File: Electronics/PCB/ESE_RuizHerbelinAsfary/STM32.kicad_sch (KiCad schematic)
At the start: 0 parts

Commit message: STM32 Symbol finished
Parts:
- added U?: STM32G070RBTx, symbol STM32G070RBTx:STM32G070RBTx
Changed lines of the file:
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@@
 (kicad_sch (version 20211123) (generator eeschema)
   (paper "A4")
+  (symbol (lib_id "STM32G070RBTx:STM32G070RBTx") (at 96.52 52.07 0) (unit 1)
+    (in_bom yes) (on_board yes)
+    (property "Reference" "U?" (id 0) (at 49.53 29.21 0))
+    (property "Value" "STM32G070RBTx" (id 1) (at 55.88 77.47 0))
+    (property "Footprint" "" (id 2) (at 96.52 52.07 0)
+      (effects (font (size 1.27 1.27)) hide)
+    )
+    (property "Datasheet" "" (id 3) (at 96.52 52.07 0)
+      (effects (font (size 1.27 1.27)) hide)
+    )
+    (pin "1")
+    (pin "10")
+    (pin "11")
+    (pin "12")
+    (pin "13")
+    (pin "14")
+    (pin "15")
+    (pin "16")
+    (pin "17")
+    (pin "18")
+    (pin "19")
+    (pin "2")
+    (pin "20")
+    (pin "21")
+    (pin "22")
+    (pin "23")
+    (pin "24")
+    (pin "25")
+    (pin "26")
+    (pin "27")
+    (pin "28")
+    (pin "29")
+    (pin "3")
+    (pin "30")
+    (pin "31")
+    (pin "32")
+    (pin "33")
+    (pin "34")
+    (pin "35")
+    (pin "36")
+    (pin "37")
+    (pin "38")
+    (pin "39")
+    (pin "4")
+    (pin "40")
+    (pin "41")
+    (pin "42")
+    (pin "43")
+    (pin "44")
+    (pin "45")
+    (pin "46")
+    (pin "47")
+    (pin "48")
+    (pin "49")
+    (pin "5")
+    (pin "50")
+    (pin "51")
+    (pin "52")
+    (pin "53")
+    (pin "54")
+    (pin "55")
+    (pin "56")
+    (pin "57")
+    (pin "58")
+    (pin "59")
+    (pin "6")
+    (pin "60")
+    (pin "61")
+    (pin "62")
+    (pin "63")
+    (pin "64")
+    (pin "7")
+    (pin "8")
+    (pin "9")
+  )
 )

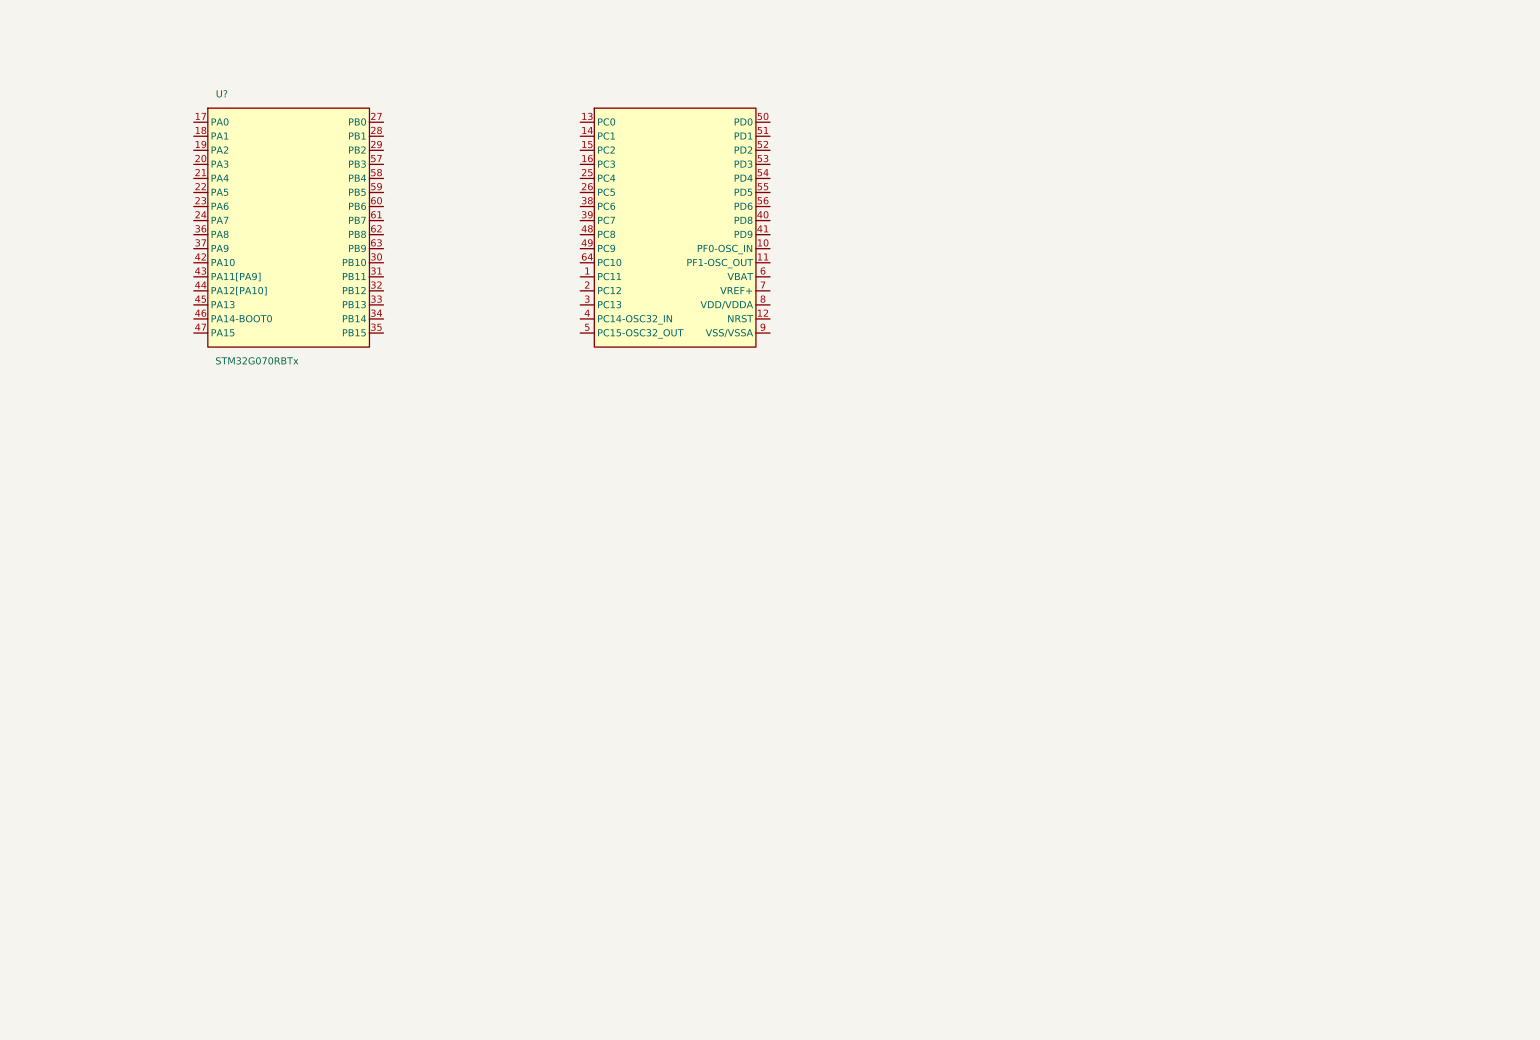
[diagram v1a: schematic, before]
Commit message: SWD connection finished
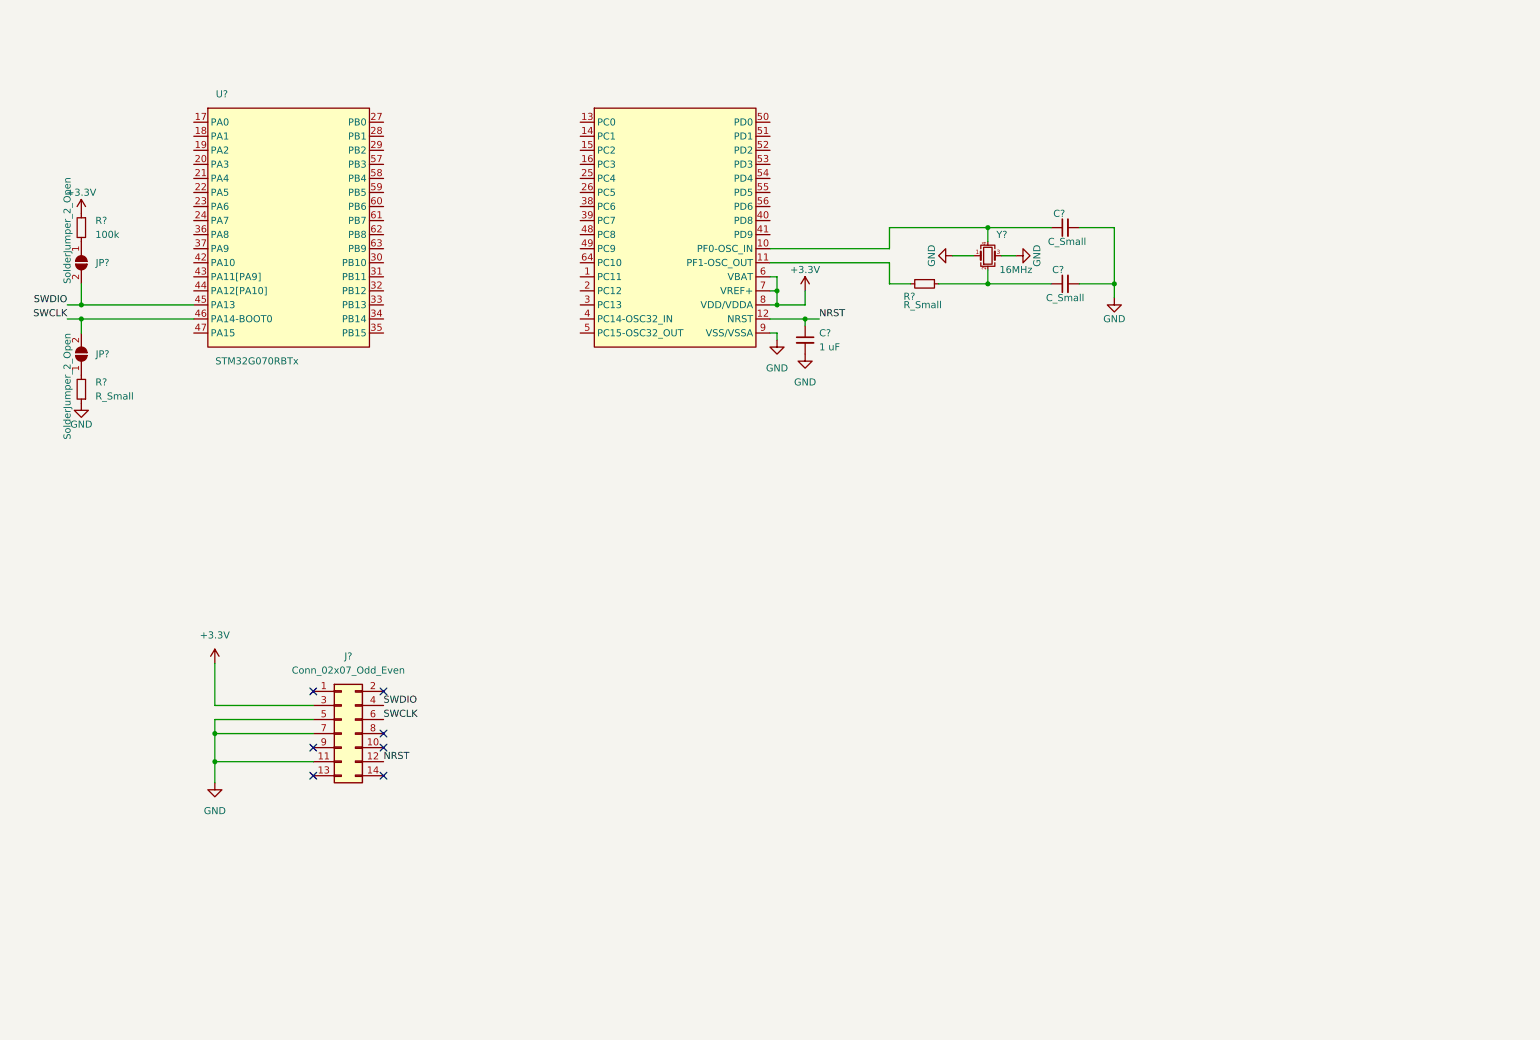
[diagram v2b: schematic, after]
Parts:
- added C? (x2): C_Small, Capacitor_SMD:C_0603_1608Metric_Pad1.08x0.95mm_HandSolder, symbol Device:C_Small
- added C?: 1 uF, symbol Device:C_Small
- added J?: Conn_02x07_Odd_Even, Connector_PinHeader_1.27mm:PinHeader_2x07_P1.27mm_Vertical_SMD, symbol Connector_Generic:Conn_02x07_Odd_Even
- added JP? (x2): SolderJumper_2_Open, symbol Jumper:SolderJumper_2_Open
- added R? (x2): R_Small, Resistor_SMD:R_0603_1608Metric_Pad0.98x0.95mm_HandSolder, symbol Device:R_Small
- added R?: 100k, Resistor_SMD:R_0603_1608Metric_Pad0.98x0.95mm_HandSolder, symbol Device:R_Small
- added Y?: 16MHz, Crystal:Crystal_SMD_EuroQuartz_MT-4Pin_3.2x2.5mm, symbol Device:Crystal_GND24_Small
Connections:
- net at U?.10 (PF0-OSC_IN): now also C?.1, Y?.4
- net at U?.11 (PF1-OSC_OUT): now also R?.2
- net NRST: now reaches U?.12 (NRST)
- net NRST: now also C?.1, J?.12 (Pin_12)
- net SWDIO: now reaches U?.45 (PA13)
- net SWDIO: now also J?.4 (Pin_4), JP?.2 (B)
- net SWCLK: now reaches U?.46 (PA14-BOOT0)
- net SWCLK: now also J?.6 (Pin_6), JP?.2 (B)
- net +3.3V: now reaches U?.6 (VBAT)
- net +3.3V: now also U?.7 (VREF+), U?.8 (VDD/VDDA), J?.3 (Pin_3), R?.1
- net GND: now reaches U?.9 (VSS/VSSA)
- net GND: now also C?.2, C?.2, C?.2, J?.11 (Pin_11), J?.5 (Pin_5), J?.7 (Pin_7), R?.1, Y?.1, Y?.3
- new net: C?.1, R?.1, Y?.2
- new net: JP?.1 (A), R?.2 (x2)
- no-connect marks 0 -> 7

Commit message: STM32 schematics done with comments and labels
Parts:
- added C?: 4.7uF, symbol Device:C_Small
- added C?: 1uF, symbol Device:C_Small
- added C? (x2): 100nF, symbol Device:C_Small
- added D?: Red, LED_SMD:LED_0603_1608Metric_Pad1.05x0.95mm_HandSolder, symbol Device:LED_Small
- added D?: Green, LED_SMD:LED_0603_1608Metric_Pad1.05x0.95mm_HandSolder, symbol Device:LED_Small
- added JP? (x2): SolderJumper_2_Open, Jumper:SolderJumper-2_P1.3mm_Open_TrianglePad1.0x1.5mm, symbol Jumper:SolderJumper_2_Open
- added L?: 600R@100MHz, symbol Device:L_Small
- added R? (x2): 1k, Resistor_SMD:R_0603_1608Metric_Pad0.98x0.95mm_HandSolder, symbol Device:R_Small
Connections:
- net +3.3V: now also D?.2 (A); no longer U?.8 (VDD/VDDA)
- net GND: now also C?.2, C?.2, C?.2, C?.2, R?.2, R?.2
- net PC11: now reaches U?.1 (PC11)
- net PC0: now reaches U?.13 (PC0)
- net PC1: now reaches U?.14 (PC1)
- net PC2: now reaches U?.15 (PC2)
- net PC3: now reaches U?.16 (PC3)
- net PA0: now reaches U?.17 (PA0)
- net PA1: now reaches U?.18 (PA1)
- net VCP_TX: now reaches U?.19 (PA2)
- net VCP_TX: now also JP?.1 (A)
- net PC12: now reaches U?.2 (PC12)
- net VCP_RX: now reaches U?.20 (PA3)
- net VCP_RX: now also JP?.1 (A)
- net PA4: now reaches U?.21 (PA4)
- net PA5: now reaches U?.22 (PA5)
- net PA6: now reaches U?.23 (PA6)
- net PA7: now reaches U?.24 (PA7)
- net PC4: now reaches U?.25 (PC4)
- net PC5: now reaches U?.26 (PC5)
- net PB0: now reaches U?.27 (PB0)
- net PB1: now reaches U?.28 (PB1)
- net PB2: now reaches U?.29 (PB2)
- net PC13: now reaches U?.3 (PC13)
- net PB10: now reaches U?.30 (PB10)
- net PB11: now reaches U?.31 (PB11)
- net PB12: now reaches U?.32 (PB12)
- net PB13: now reaches U?.33 (PB13)
- net PB14: now reaches U?.34 (PB14)
- net PB15: now reaches U?.35 (PB15)
- net PA8: now reaches U?.36 (PA8)
- net PA9: now reaches U?.37 (PA9)
- net PC6: now reaches U?.38 (PC6)
- net PC7: now reaches U?.39 (PC7)
- net PC14: now reaches U?.4 (PC14-OSC32_IN)
- net PD8: now reaches U?.40 (PD8)
- net PD9: now reaches U?.41 (PD9)
- net PA10: now reaches U?.42 (PA10)
- net PA11: now reaches U?.43 (PA11[PA9])
- net PA12: now reaches U?.44 (PA12[PA10])
- net PA15: now reaches U?.47 (PA15)
- net PC8: now reaches U?.48 (PC8)
- net PC9: now reaches U?.49 (PC9)
- net PC15: now reaches U?.5 (PC15-OSC32_OUT)
- net PD0: now reaches U?.50 (PD0)
- net PD1: now reaches U?.51 (PD1)
- net PD2: now reaches U?.52 (PD2)
- net PD3: now reaches U?.53 (PD3)
- net PD4: now reaches U?.54 (PD4)
- net PD5: now reaches U?.55 (PD5)
- net PD6: now reaches U?.56 (PD6)
- net PB3: now reaches U?.57 (PB3)
- net PB4: now reaches U?.58 (PB4)
- net PB5: now reaches U?.59 (PB5)
- net PB6: now reaches U?.60 (PB6)
- net PB7: now reaches U?.61 (PB7)
- net PB8: now reaches U?.62 (PB8)
- net PB9: now reaches U?.63 (PB9)
- net PC10: now reaches U?.64 (PC10)
- net at J?.13 (Pin_13): now also JP?.2 (B)
- net at J?.14 (Pin_14): now also JP?.2 (B)
- new net: D?.1 (K), R?.1 (x2)
- new net +5V: D?.2 (A)
- new net VDD: C?.1, C?.1, C?.1, L?.2
- new net VDDA: C?.1, L?.1, U?.8 (VDD/VDDA)
- no-connect marks 7 -> 5
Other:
- note added: "BYPASS Capacitor"
- note added: "Power LED"
- note added: "STM32F070"
- note added: "Serial Wire Debug"
- note added: "The Bypass capacitor must be placed near the corresponding power input"
- note added: "close to VBAT"
- note added: "close to VDD"
- note added: "close to VREF"
- moved on the sheet: C?, J?, JP?, R?, U?, Y?
